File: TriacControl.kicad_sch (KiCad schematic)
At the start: 53 parts, among them J1 AC LINE, J2 LOAD, J3 ZEROCROSS, J4 PWM, Q1 BTA16-600, Q2 2N2907, U1 MOC3023, U2 PC817, U3 PC817

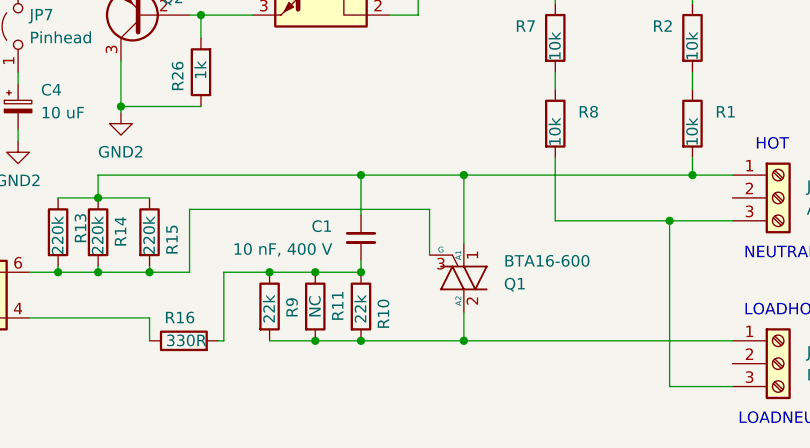
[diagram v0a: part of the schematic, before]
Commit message: Updated TRIAC and snubber circuit
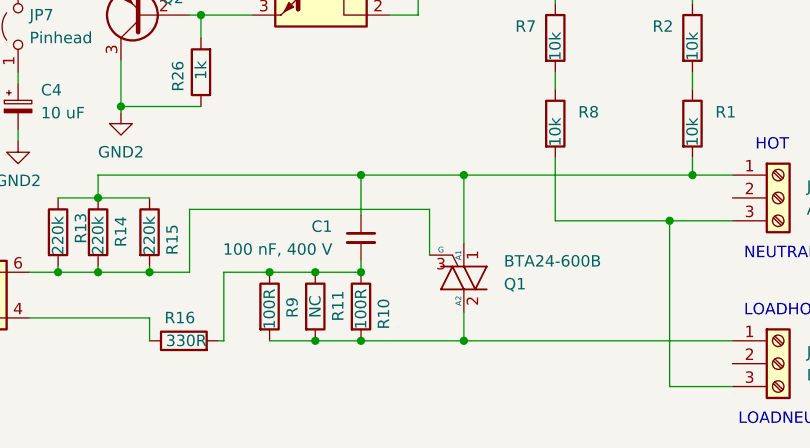
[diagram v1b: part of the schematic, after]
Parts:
- C1: value 10 nF, 400 V -> 100 nF, 400 V
- Q1: value BTA16-600 -> BTA24-600B
- R10, R9: value 22k -> 100R
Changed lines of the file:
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@@
       (effects (font (size 1.27 1.27)) (justify left))
     )
-    (property "Value" "22k" (at 162.56 130.175 90)
+    (property "Value" "100R" (at 162.56 130.81 90)
       (effects (font (size 1.27 1.27)) (justify left))
     )
@@
       (effects (font (size 1.27 1.27)) (justify left))
     )
-    (property "Value" "22k" (at 152.4 130.175 90)
+    (property "Value" "100R" (at 152.4 130.81 90)
       (effects (font (size 1.27 1.27)) (justify left))
     )
@@
       (effects (font (size 1.27 1.27)) (justify left))
     )
-    (property "Value" "BTA16-600" (at 178.435 123.2408 0)
+    (property "Value" "BTA24-600B" (at 178.435 123.2408 0)
       (effects (font (size 1.27 1.27)) (justify left))
     )
@@
       (effects (font (size 1.27 1.27)) (justify left))
     )
-    (property "Value" "10 nF, 400 V" (at 159.385 121.9263 0)
-      (effects (font (size 1.27 1.27)) (justify left))
-    )
+    (property "Value" "100 nF, 400 V" (at 159.385 121.9263 0)
+      (effects (font (size 1.27 1.27)) (justify left))
+    )
